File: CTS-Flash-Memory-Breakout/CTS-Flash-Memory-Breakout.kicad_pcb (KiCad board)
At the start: 2 copper layers, 44.2 x 24 mm, 10 parts, among them J1 Conn_02x07_Counter_Clockwise, U1 S70FL01GSAGMFI011

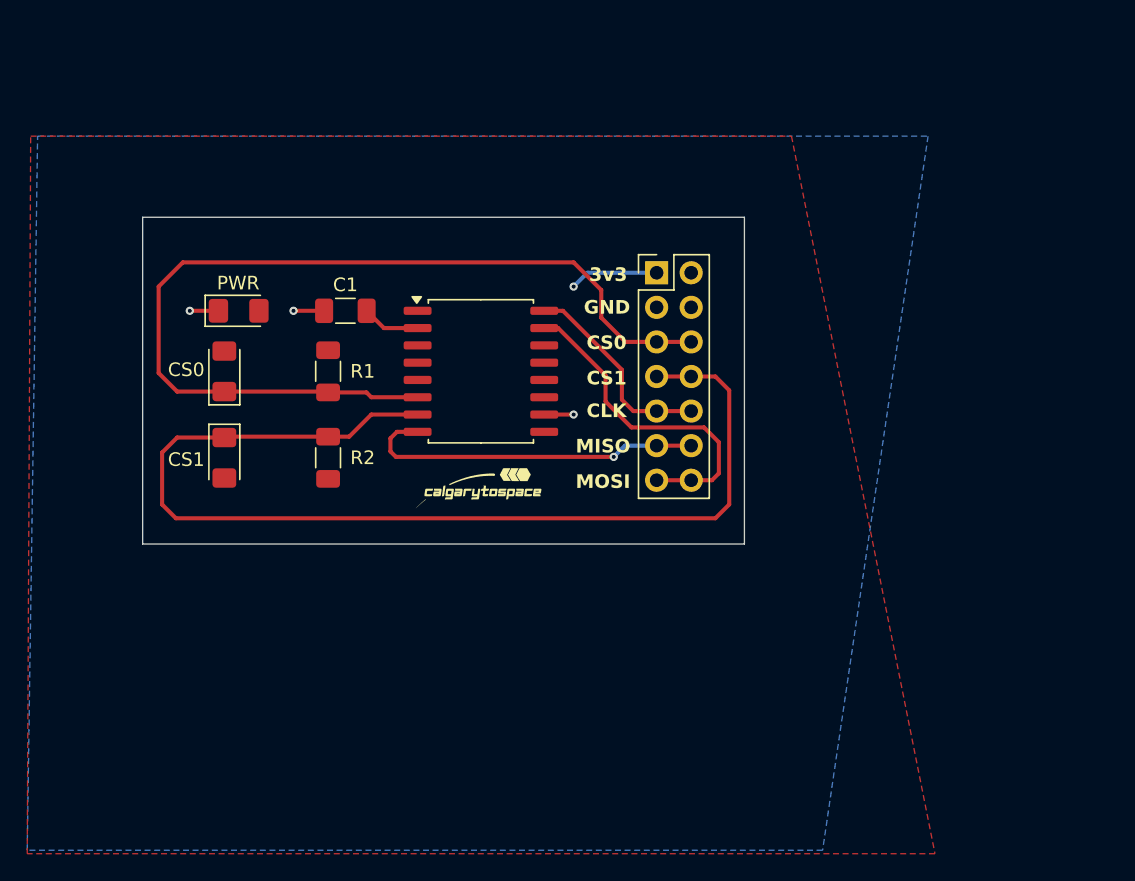
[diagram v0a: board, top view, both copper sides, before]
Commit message: Create Rev 2 board
- Breakout every pin on the chip to new headers
- Fix missing inline resistors for LEDs
- Add extra bulk capacitance
- Reroute with wide traces
- More silkscreens
- Silkscreens for writing notes/labels in Sharpie
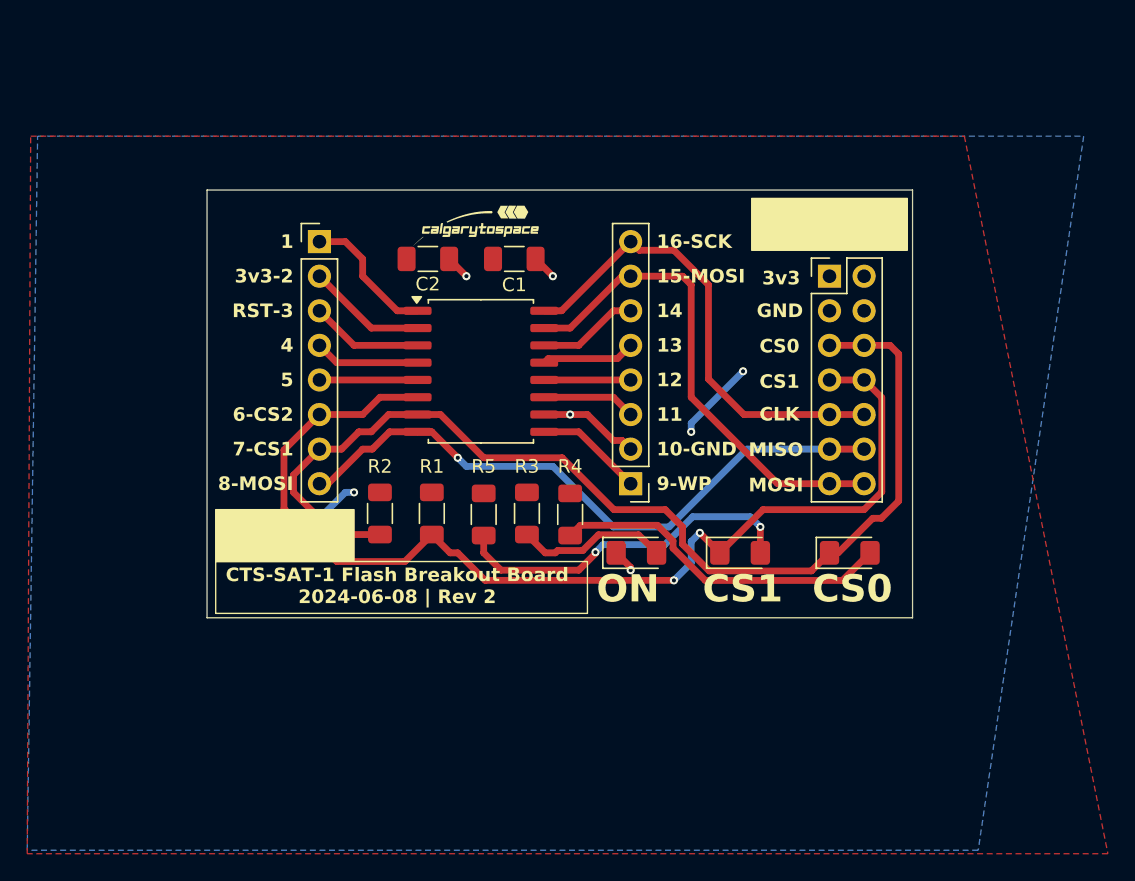
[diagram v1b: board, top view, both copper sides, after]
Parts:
- removed CS0, CS1: LED, LED_SMD:LED_1206_3216Metric_Pad1.42x1.75mm_HandSolder
- added C2: 1u, Capacitor_SMD:C_1206_3216Metric_Pad1.33x1.80mm_HandSolder, F.Cu at (141.9, 73.7)
- added D2: LED, LED_SMD:LED_1206_3216Metric_Pad1.42x1.75mm_HandSolder, F.Cu at (172.9, 95.2)
- added D3: LED, LED_SMD:LED_1206_3216Metric_Pad1.42x1.75mm_HandSolder, F.Cu at (164.9, 95.2)
- added J2: Conn_01x08, Connector_PinHeader_2.54mm:PinHeader_1x08_P2.54mm_Vertical, F.Cu at (156.8, 90.2)
- added J3: Conn_01x08, Connector_PinHeader_2.54mm:PinHeader_1x08_P2.54mm_Vertical, F.Cu at (134.0, 72.4)
- added R3: 5k, Resistor_SMD:R_1206_3216Metric_Pad1.30x1.75mm_HandSolder, F.Cu at (149.2, 92.4)
- added R4: 5k, Resistor_SMD:R_1206_3216Metric_Pad1.30x1.75mm_HandSolder, F.Cu at (152.4, 92.4)
- added R5: 5k, Resistor_SMD:R_1206_3216Metric_Pad1.30x1.75mm_HandSolder, F.Cu at (146.1, 92.4)
- moved D1 34.2 mm to (157.3, 95.2)
- moved G*** 19.3 mm to (145.4, 71.1)
- moved C1 13.0 mm to (148.3, 73.7), turned to 180 degrees
- moved R1 12.9 mm to (142.2, 92.4)
- moved J1 12.7 mm to (171.4, 74.9)
- moved G*** 8.82 mm to (145.7, 81.9)
- moved R2 5.59 mm to (138.4, 92.4), turned to 90 degrees
- renumbered PWR to D1
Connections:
- D1 pad 2: +3V3 -> Net-(D1-A)
- R1 pad 2: SPI_NCS_FLASH0 -> SPI_NCS_FLASH1
- R2 pad 1: SPI_NCS_FLASH1 -> SPI_NCS_FLASH0
- U1 pad 1: unconnected-(U1-*HOLD/IO3-Pad1) -> Net-(J3-Pin_1)
- U1 pad 11: unconnected-(U1-DNU-Pad11) -> Net-(J2-Pin_3)
- U1 pad 12: unconnected-(U1-DNU-Pad12) -> Net-(J2-Pin_4)
- U1 pad 13: unconnected-(U1-NC-Pad13) -> Net-(J2-Pin_5)
- U1 pad 14: unconnected-(U1-VIO/RFU-Pad14) -> Net-(J2-Pin_6)
- U1 pad 3: unconnected-(U1-*RESET/RFU-Pad3) -> Net-(J3-Pin_3)
- U1 pad 4: unconnected-(U1-DNU-Pad4) -> Net-(J3-Pin_4)
- U1 pad 5: unconnected-(U1-DNU-Pad5) -> Net-(J3-Pin_5)
- U1 pad 6: SPI_NCS_FLASH0 -> SPI_NCS_FLASH1
- U1 pad 7: SPI_NCS_FLASH1 -> SPI_NCS_FLASH0
- U1 pad 9: unconnected-(U1-*WP/IO2-Pad9) -> Net-(J2-Pin_1)
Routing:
- net Net-(D3-A): track 0.00 -> 26.0 mm, vias 0 -> 2
- net Net-(D2-A): track 0.00 -> 25.2 mm
- net SPI_MISO: track 25.8 -> 46.8 mm
- net SPI_CLK: track 15.1 -> 34.9 mm
- net SPI_MOSI: track 24.5 -> 36.2 mm
- net +3V3: track 10.8 -> 22.4 mm, vias 1 -> 4
- net Net-(D1-A): track 0.00 -> 11.2 mm
- net Net-(J3-Pin_1): track 0.00 -> 10.1 mm
- net SPI_NCS_FLASH0: track 69.6 -> 79.0 mm
- net Net-(J3-Pin_3): track 0.00 -> 8.26 mm
- net Net-(J2-Pin_1): track 0.00 -> 7.93 mm
- net Net-(J3-Pin_4): track 0.00 -> 7.74 mm
- net Net-(J2-Pin_6): track 0.00 -> 7.40 mm
- net Net-(J3-Pin_5): track 0.00 -> 7.21 mm
- net Net-(J2-Pin_3): track 0.00 -> 6.88 mm
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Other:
- board size 44.2 x 24 mm -> 51.8 x 31.4 mm
- board text added: "1"
- board text added: "10-GND"
- board text added: "11"
- board text added: "12"
- board text added: "13"
- board text added: "14"
- board text added: "15-MOSI"
- board text added: "16-SCK"
- board text added: "3v3-2"
- board text added: "4"
- board text added: "5"
- board text added: "6-CS2"
- board text added: "7-CS1"
- board text added: "8-MOSI"
- board text added: "9-WP"
- board text added: "CTS-SAT-1 Flash Breakout Board 2024-06-08 | Rev 2"
- board text added: "ON"
- board text added: "RST-3"
- board text removed: "2024-05-27 Rev. 1"

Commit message: Create Rev 2
- Add mounting holes
- Improve routing
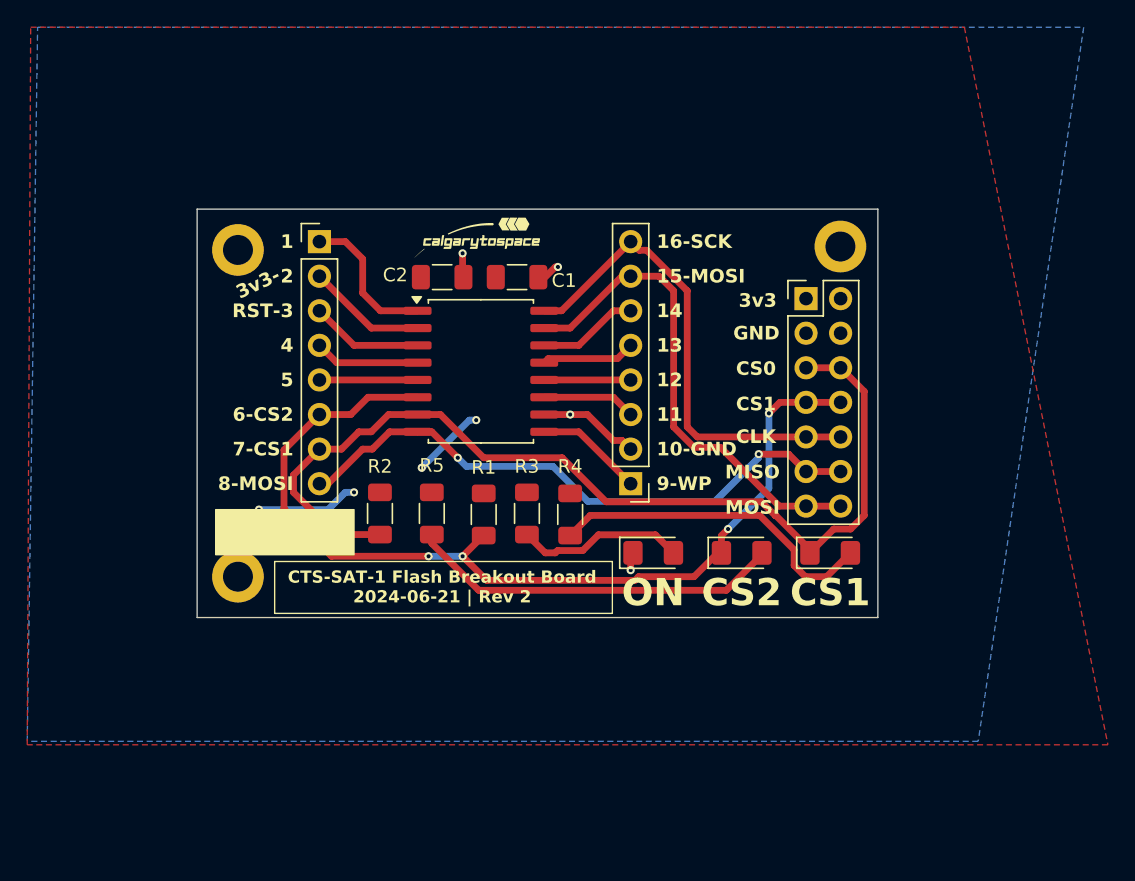
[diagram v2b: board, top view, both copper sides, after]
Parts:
- added H1: MountingHole_Pad, MountingHole:MountingHole_2.2mm_M2_DIN965_Pad, F.Cu at (128.0, 73.0)
- added H2: MountingHole_Pad, MountingHole:MountingHole_2.2mm_M2_DIN965_Pad, F.Cu at (128.0, 97.0)
- added H3: MountingHole_Pad, MountingHole:MountingHole_2.2mm_M2_DIN965_Pad, F.Cu at (172.2, 72.8)
- moved R1 3.81 mm to (146.1, 92.4)
- moved R5 3.81 mm to (142.2, 92.4)
- moved J1 2.38 mm to (169.7, 76.6)
- moved C2 1.70 mm to (143.0, 75.0)
- moved D2 1.44 mm to (171.5, 95.2)
- moved C1 1.36 mm to (148.5, 75.0)
- moved D1 1.24 mm to (158.5, 95.2)
- moved G*** 0.88 mm to (145.5, 72.0)
- moved D3 0.12 mm to (165.0, 95.2)
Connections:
- D2 pad 1: SPI_NCS_FLASH0 -> SPI_NCS_FLASH1
- D3 pad 1: SPI_NCS_FLASH1 -> SPI_NCS_FLASH2
- J1 pad 5: SPI_NCS_FLASH0 -> SPI_NCS_FLASH1
- J1 pad 6: SPI_NCS_FLASH0 -> SPI_NCS_FLASH1
- J1 pad 7: SPI_NCS_FLASH1 -> SPI_NCS_FLASH2
- J1 pad 8: SPI_NCS_FLASH1 -> SPI_NCS_FLASH2
- J3 pad 6: SPI_NCS_FLASH1 -> SPI_NCS_FLASH2
- J3 pad 7: SPI_NCS_FLASH0 -> SPI_NCS_FLASH1
- R1 pad 2: SPI_NCS_FLASH1 -> SPI_NCS_FLASH2
- R2 pad 1: SPI_NCS_FLASH0 -> SPI_NCS_FLASH1
- U1 pad 6: SPI_NCS_FLASH1 -> SPI_NCS_FLASH2
- U1 pad 7: SPI_NCS_FLASH0 -> SPI_NCS_FLASH1
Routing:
- net SPI_NCS_FLASH0: track 79.0 -> 0.00 mm
- net SPI_NCS_FLASH2: track 0.00 -> 70.4 mm, vias 0 -> 4
- net SPI_NCS_FLASH1: track 79.6 -> 72.3 mm, vias 2 -> 0
- net SPI_MISO: track 46.8 -> 44.3 mm, vias 1 -> 2
- net Net-(D3-A): track 26.0 -> 27.5 mm, vias 2 -> 0
- net Net-(D1-A): track 11.2 -> 12.4 mm
- net GND: track 12.7 -> 11.8 mm
- net SPI_CLK: track 34.9 -> 35.7 mm
- net Net-(J3-Pin_1): track 10.1 -> 10.8 mm
- net Net-(D2-A): track 25.2 -> 24.5 mm
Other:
- board size 51.8 x 31.4 mm -> 50 x 30 mm
- board text added: "2"
- board text added: "3v3-"
- board text added: "CS2"
- board text added: "CTS-SAT-1 Flash Breakout Board ${ISSUE_DATE} | ${REVISION}"
- board text added: "Top Layer (Red) - 3V3 Bottom Layer (Blue) - GND"
- board text removed: "3v3-2"
- board text removed: "CTS-SAT-1 Flash Breakout Board 2024-06-08 | Rev 2"

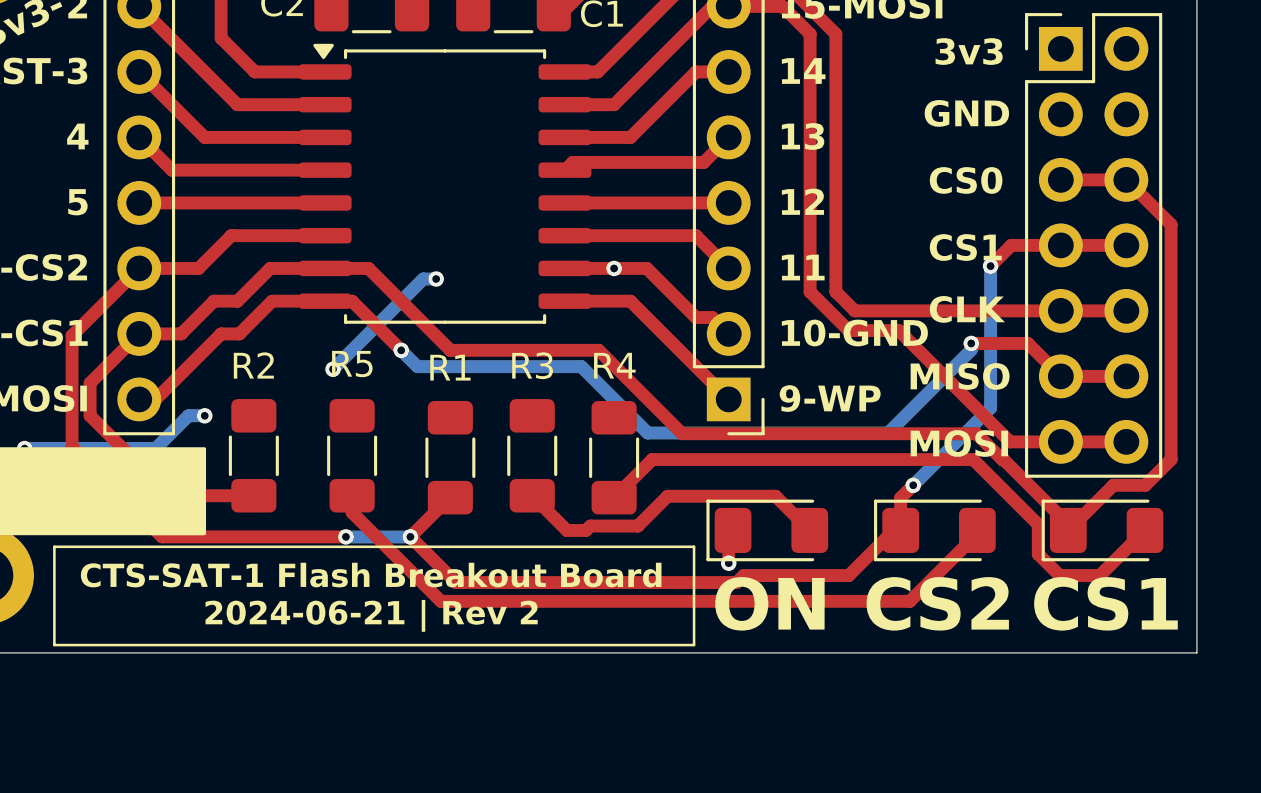
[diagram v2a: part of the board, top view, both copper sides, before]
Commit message: Create Rev 3 with CS label fix, teardrops
Changes from Rev 2:
	* Fixed bad CS0/CS1 label to CS1/CS2.
	* Added teardrops
	* Fixed some routing to move traces farther from pads
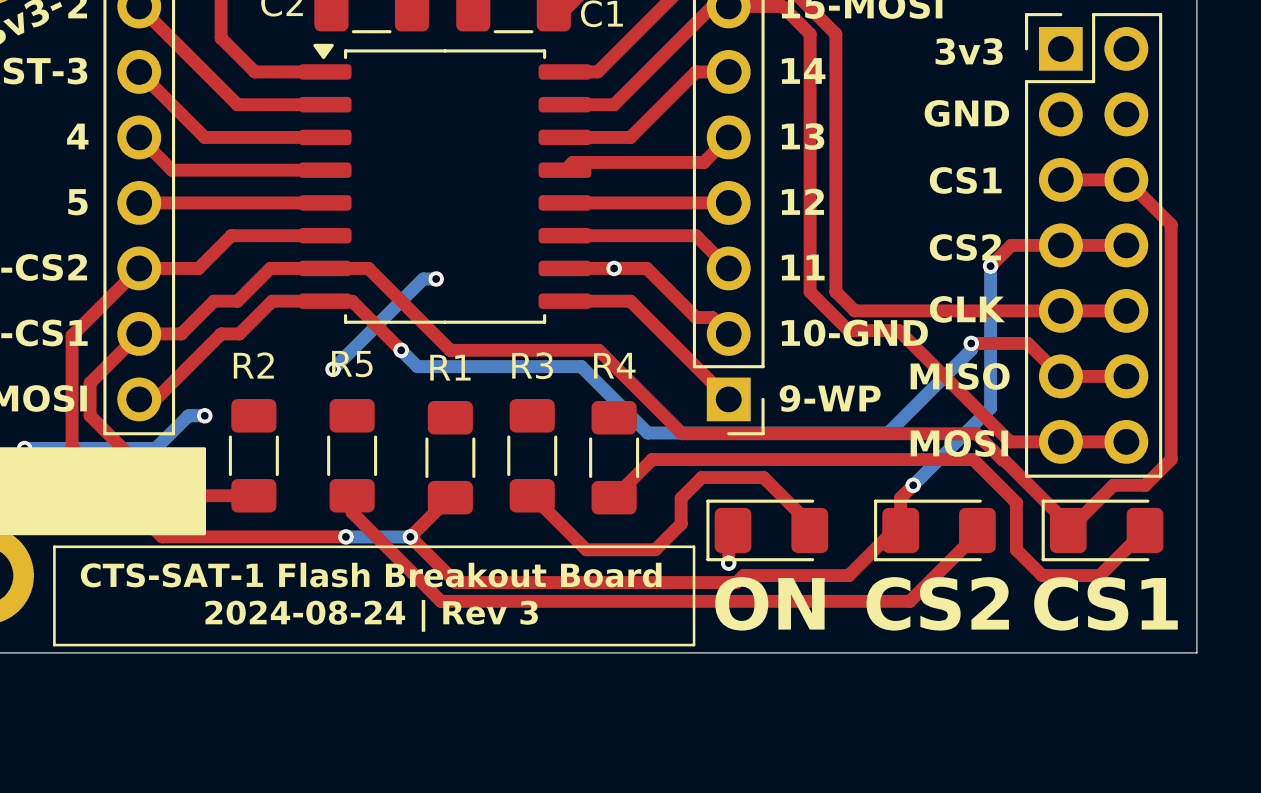
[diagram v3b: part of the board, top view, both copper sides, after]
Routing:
- net Net-(D1-A): track 12.4 -> 14.4 mm
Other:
- board text removed: "CS0"
